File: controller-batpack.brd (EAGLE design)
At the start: 31.4 x 25.4 mm, 13 parts

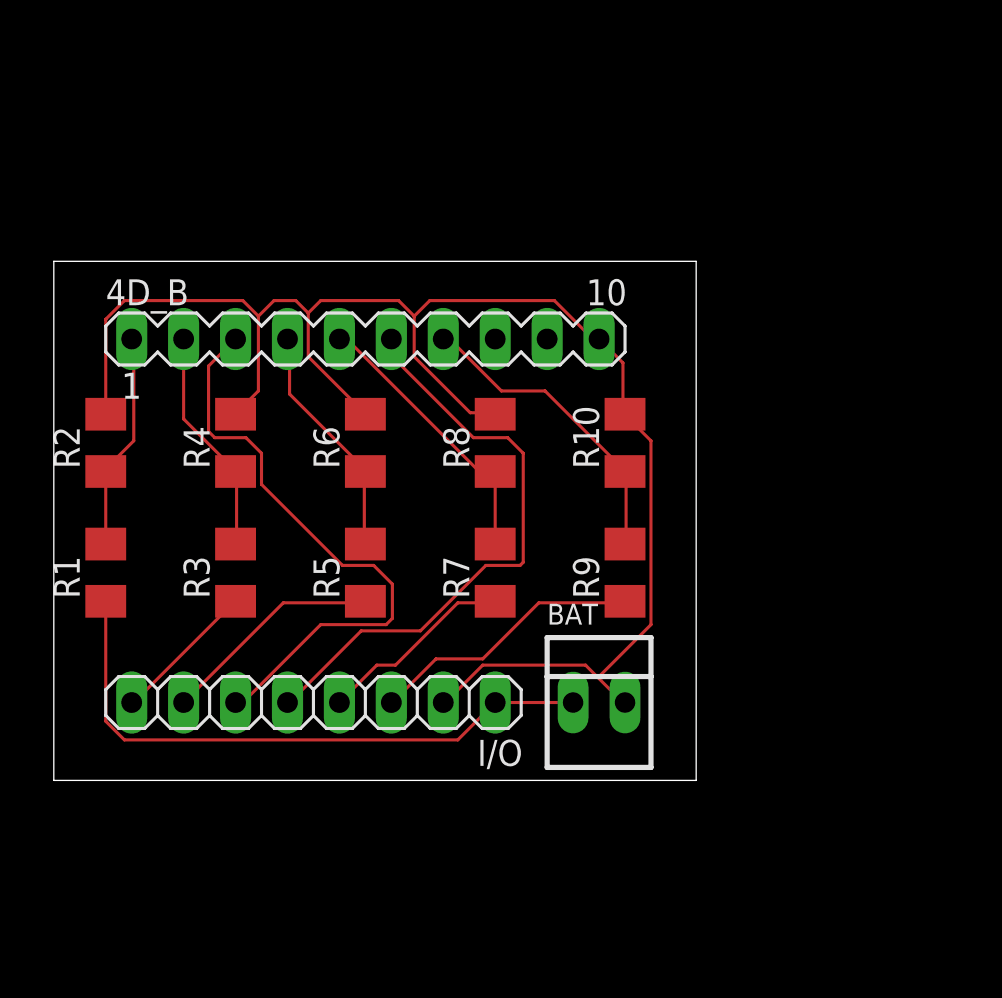
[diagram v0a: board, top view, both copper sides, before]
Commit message: updated battery pack board
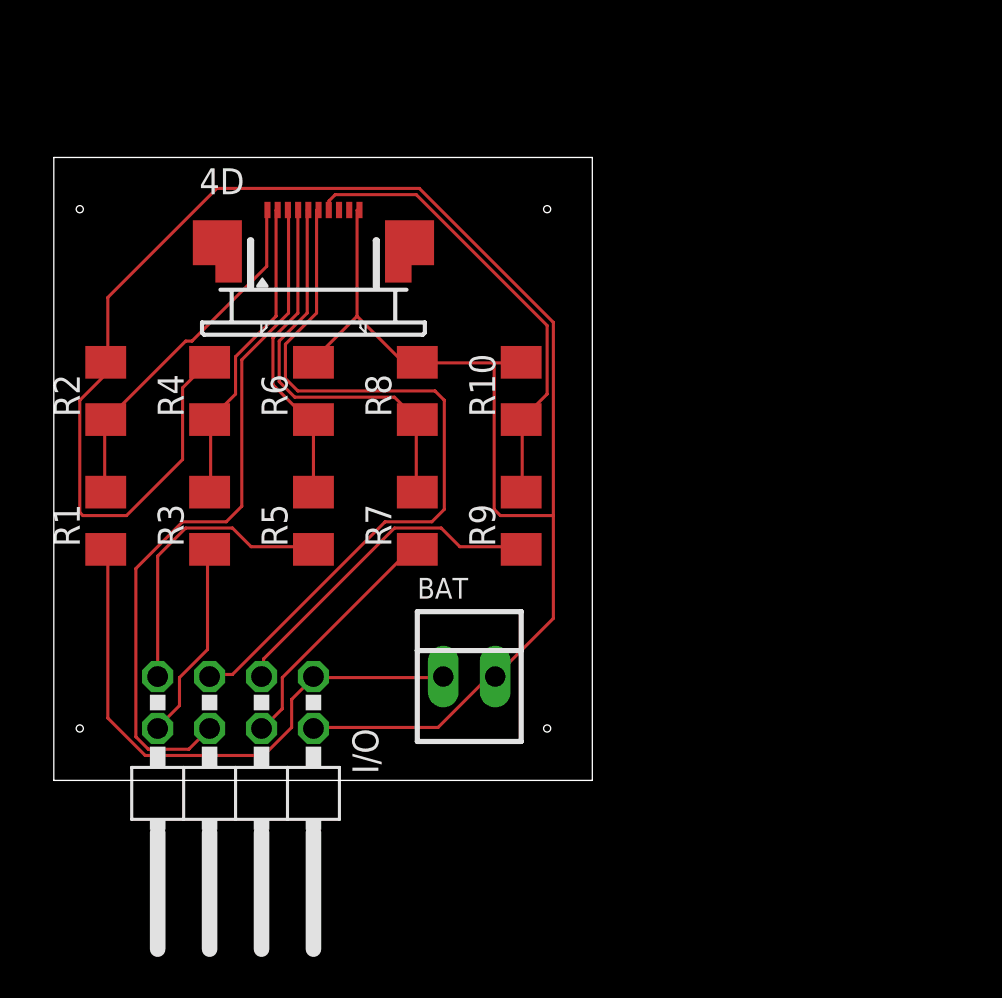
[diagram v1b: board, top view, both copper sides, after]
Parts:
- removed 4D_B: (no value), con-lstb:MA10-1
- added 4D: (no value), con-molex:52745-1090
- I/O: device pinhead:1X08 -> pinhead:2X04/90
- moved BAT 6.48 mm to (20.3, 5.08)
- moved I/O 6.35 mm to (8.89, -1.27)
- moved R10 5.68 mm to (22.9, 19.1)
- moved R9 5.68 mm to (22.9, 12.7)
- moved R7 4.58 mm to (17.8, 12.7)
- moved R8 4.58 mm to (17.8, 19.1)
- moved R5 3.59 mm to (12.7, 12.7)
- moved R6 3.59 mm to (12.7, 19.1)
- moved R3 2.84 mm to (7.62, 12.7)
- moved R4 2.84 mm to (7.62, 19.1)
- moved R1 2.54 mm to (2.54, 12.7)
- moved R2 2.54 mm to (2.54, 19.1)
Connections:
- net 3.3V: now also 4D.1; no longer 4D_B.1
- net 4D_CS_L: now also 4D.5; no longer 4D_B.5
- net 4D_INT: now also 4D.6; no longer 4D_B.6
- net 4D_PD_L: now also 4D.7; no longer 4D_B.7
- net GND: now also 4D.10; no longer 4D_B.10
- net MISO: now also 4D.3; no longer 4D_B.3
- net MOSI_L: now also 4D.4; no longer 4D_B.4
- net SCK_L: now also 4D.2; no longer 4D_B.2
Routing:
- net GND: track 79.3 -> 105.5 mm
- net 4D_INT: track 28.9 -> 37.4 mm
- net 4D_PD_L: track 15.2 -> 22.6 mm
- net 3.3V: track 10.6 -> 17.3 mm
- net 4D_CS_L: track 14.0 -> 20.1 mm
- net MISO: track 29.1 -> 34.4 mm
- net SCK_L: track 11.1 -> 15.3 mm
- net MOSI_L: track 11.7 -> 15.3 mm
- net MOSI: track 10.9 -> 14.6 mm
- net 4D_PD: track 13.5 -> 16.6 mm
- net SCK: track 7.12 -> 9.85 mm
- net 4D_CS: track 9.71 -> 12.1 mm
- net 5V: track 29.9 -> 27.9 mm
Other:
- board size 31.4 x 25.4 mm -> 26.3 x 30.5 mm

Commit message: Created V2 main board, updated second board
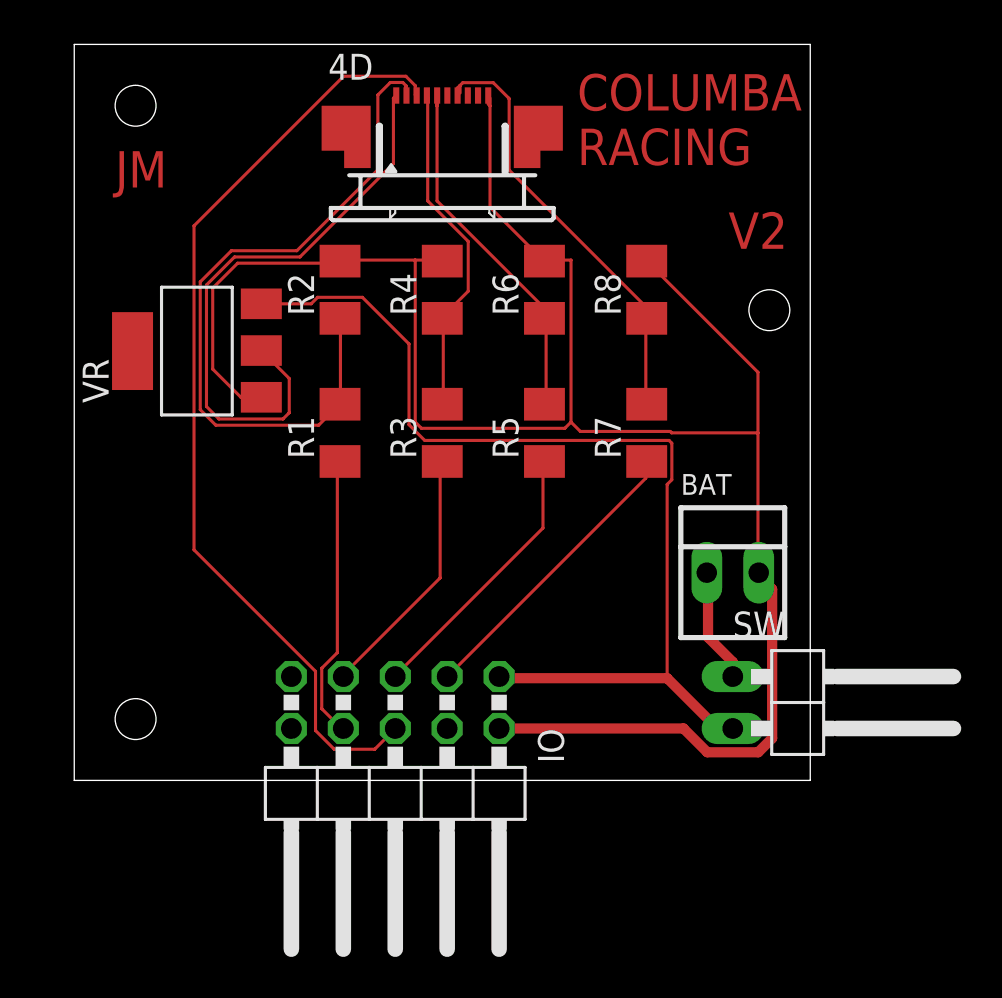
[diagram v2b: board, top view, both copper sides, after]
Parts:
- removed I/O: (no value), pinhead:2X04/90
- removed R10: 2k, rcl:M1206
- removed R9: 1k, rcl:M1206
- added IO: (no value), pinhead:2X05/90
- added SW: (no value), pinhead:1X02/90
- added VR: REG1117, burr-brown:SOT223
- moved BAT 13.9 mm to (33.2, 10.2)
- moved R2 12.5 mm to (14.0, 24.0)
- moved R4 12.4 mm to (19.0, 24.0)
- moved R6 12.3 mm to (24.0, 24.0)
- moved R8 12.3 mm to (29.0, 24.0)
- moved R1 12.2 mm to (14.0, 17.0)
- moved R3 12.2 mm to (19.0, 17.0)
- moved R5 12.1 mm to (24.0, 17.0)
- moved R7 12.0 mm to (29.0, 17.0)
- moved 4D 8.43 mm to (19.0, 31.0)
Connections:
- removed net 4D_INT: 4D.6, I/O.5
- new net 5V2: BAT.1, SW.1
- net 3.3V: now also VR.2; no longer R1.2, R2.1
- net 4D_CS: now also IO.5, R5.1; no longer I/O.4, R7.1
- net 4D_CS_L: now also R5.2, R6.1; no longer R7.2, R8.1
- net 4D_PD: now also IO.3, R7.1; no longer I/O.3, R9.1
- net 4D_PD_L: now also R7.2, R8.1; no longer R10.1, R9.2
- net 5V: now also IO.1, SW.2, VR.3; no longer BAT.1, I/O.1, R1.1
- net GND: now also IO.2, VR.1; no longer I/O.2, R10.2
- net MISO: now also IO.6; no longer I/O.6
- net MOSI: now also IO.7, R3.1; no longer I/O.7, R5.1
- net MOSI_L: now also R3.2, R4.1; no longer R5.2, R6.1
- net SCK: now also IO.8, R1.1; no longer I/O.8, R3.1
- net SCK_L: now also R1.2, R2.1; no longer R3.2, R4.1
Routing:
- net 4D_INT: track 37.4 -> 0.00 mm
- net 5V: track 27.9 -> 49.6 mm
- net SCK_L: track 15.3 -> 35.3 mm
- net MISO: track 34.4 -> 46.4 mm
- net 3.3V: track 17.3 -> 29.0 mm
- net 5V2: track 0.00 -> 5.61 mm
- net SCK: track 9.85 -> 13.9 mm
- net GND: track 105.5 -> 103.0 mm
- net 4D_CS_L: track 20.1 -> 17.7 mm
- net MOSI: track 14.6 -> 12.5 mm
- net 4D_PD: track 16.6 -> 14.6 mm
- net 4D_CS: track 12.1 -> 13.5 mm
- net MOSI_L: track 15.3 -> 16.5 mm
- net 4D_PD_L: track 22.6 -> 21.5 mm
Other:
- board size 26.3 x 30.5 mm -> 36 x 36 mm
- board text added: "COLUMBA RACING"
- board text added: "JM"
- board text added: "V2"
